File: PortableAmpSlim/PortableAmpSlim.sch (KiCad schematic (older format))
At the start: 20 parts, among them J1 Conn_01x04_Male, J2 Speaker, Q1 MPF102, SW1 Power, U1 LM386

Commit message: Fixed footprints and replotted Gerber files
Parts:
- C5: footprint libraries:C_Flat_L7.2_H6.5 -> Capacitor_THT:CP_Radial_D10.0mm_P5.00mm
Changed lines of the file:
@@
 F 0 "C5" V 6255 2900 50  0000 C CNN
 F 1 "220uF" V 6164 2900 50  0000 C CNN
-F 2 "libraries:C_Flat_L7.2_H6.5" H 6038 2750 50  0001 C CNN
+F 2 "Capacitor_THT:CP_Radial_D10.0mm_P5.00mm" H 6038 2750 50  0001 C CNN
 F 3 "~" H 6000 2900 50  0001 C CNN
 	1    6000 2900

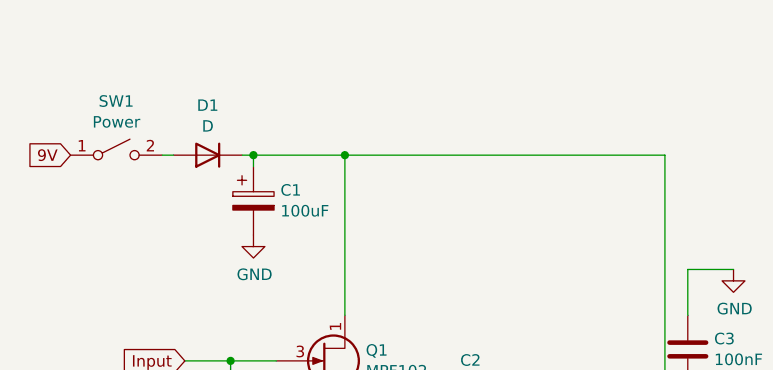
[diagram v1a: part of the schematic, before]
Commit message: Added LED
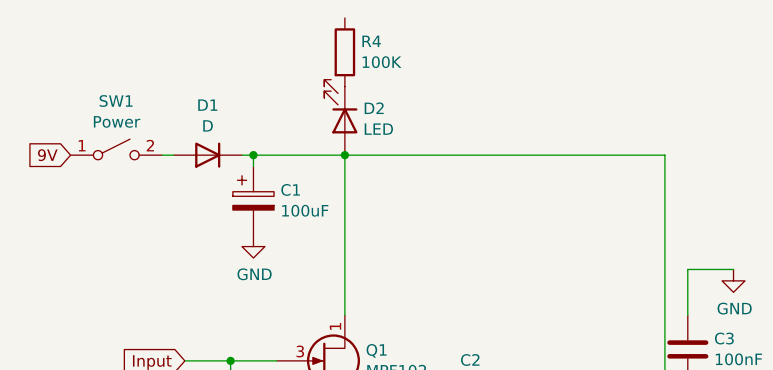
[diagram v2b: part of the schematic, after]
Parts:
- added D2: LED, LED_THT:LED_D5.0mm, symbol Device:LED
- added R4: 100K, Resistor_THT:R_Axial_DIN0207_L6.3mm_D2.5mm_P10.16mm_Horizontal, symbol Device:R
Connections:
- net at C1.1, D1.1 (K), Q1.1 (D)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: now also D2.2 (A)
- new net: D2.1 (K), R4.2
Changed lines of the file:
@@
+	1    0    0    -1
+$EndComp
+$Comp
+L Device:LED D2
+U 1 1 6083C65A
+P 3400 1450
+F 0 "D2" V 3347 1530 50  0000 L CNN
+F 1 "LED" V 3438 1530 50  0000 L CNN
+F 2 "LED_THT:LED_D5.0mm" H 3400 1450 50  0001 C CNN
+F 3 "~" H 3400 1450 50  0001 C CNN
+	1    3400 1450
+	0    1    1    0
+$EndComp
+$Comp
+L Device:R R4
+U 1 1 6083D105
+P 3400 1150
+F 0 "R4" H 3470 1196 50  0000 L CNN
+F 1 "100K" H 3470 1105 50  0000 L CNN
+F 2 "Resistor_THT:R_Axial_DIN0207_L6.3mm_D2.5mm_P10.16mm_Horizontal" V 3330 1150 50  0001 C CNN
+F 3 "~" H 3400 1150 50  0001 C CNN
+	1    3400 1150
 	1    0    0    -1
 $EndComp

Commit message: Minor changes
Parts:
- R4: value 100K -> LED
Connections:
- net GND: now also R4.1
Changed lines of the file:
@@
 P 3400 1150
 F 0 "R4" H 3470 1196 50  0000 L CNN
-F 1 "100K" H 3470 1105 50  0000 L CNN
+F 1 "LED" H 3470 1105 50  0000 L CNN
 F 2 "Resistor_THT:R_Axial_DIN0207_L6.3mm_D2.5mm_P10.16mm_Horizontal" V 3330 1150 50  0001 C CNN
 F 3 "~" H 3400 1150 50  0001 C CNN
@@
 	1    0    0    -1
 $EndComp
+$Comp
+L power:GND #PWR?
+U 1 1 61364894
+P 3150 850
+F 0 "#PWR?" H 3150 600 50  0001 C CNN
+F 1 "GND" H 3155 677 50  0000 C CNN
+F 2 "" H 3150 850 50  0001 C CNN
+F 3 "" H 3150 850 50  0001 C CNN
+	1    3150 850
+	1    0    0    -1
+$EndComp
+Wire Wire Line
+	3150 850  3400 850
+Wire Wire Line
+	3400 850  3400 1000
 $EndSCHEMATC
